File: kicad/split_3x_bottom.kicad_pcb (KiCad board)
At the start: 2 copper layers, 127.3 x 121.2 mm, 4 parts

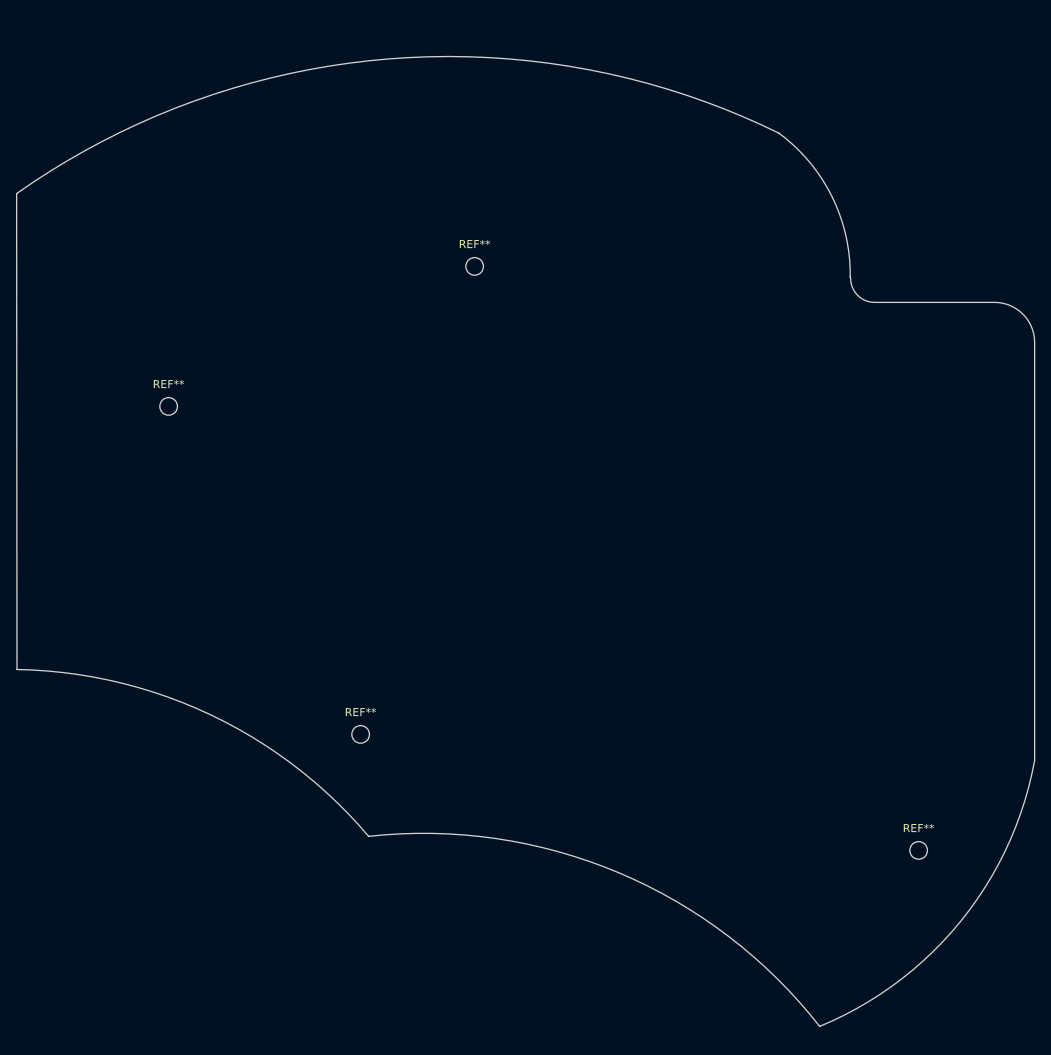
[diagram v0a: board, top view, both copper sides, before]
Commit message: added support for the pimoroni trackball breakout, changed a bunch of things, rewired the pcb, changed the bottom plate to be prettier, added some silkscreen, changed the position of one of the mounting holes, changed the angle of the trrs jacks to be properly aligned, changed the top plate to look better
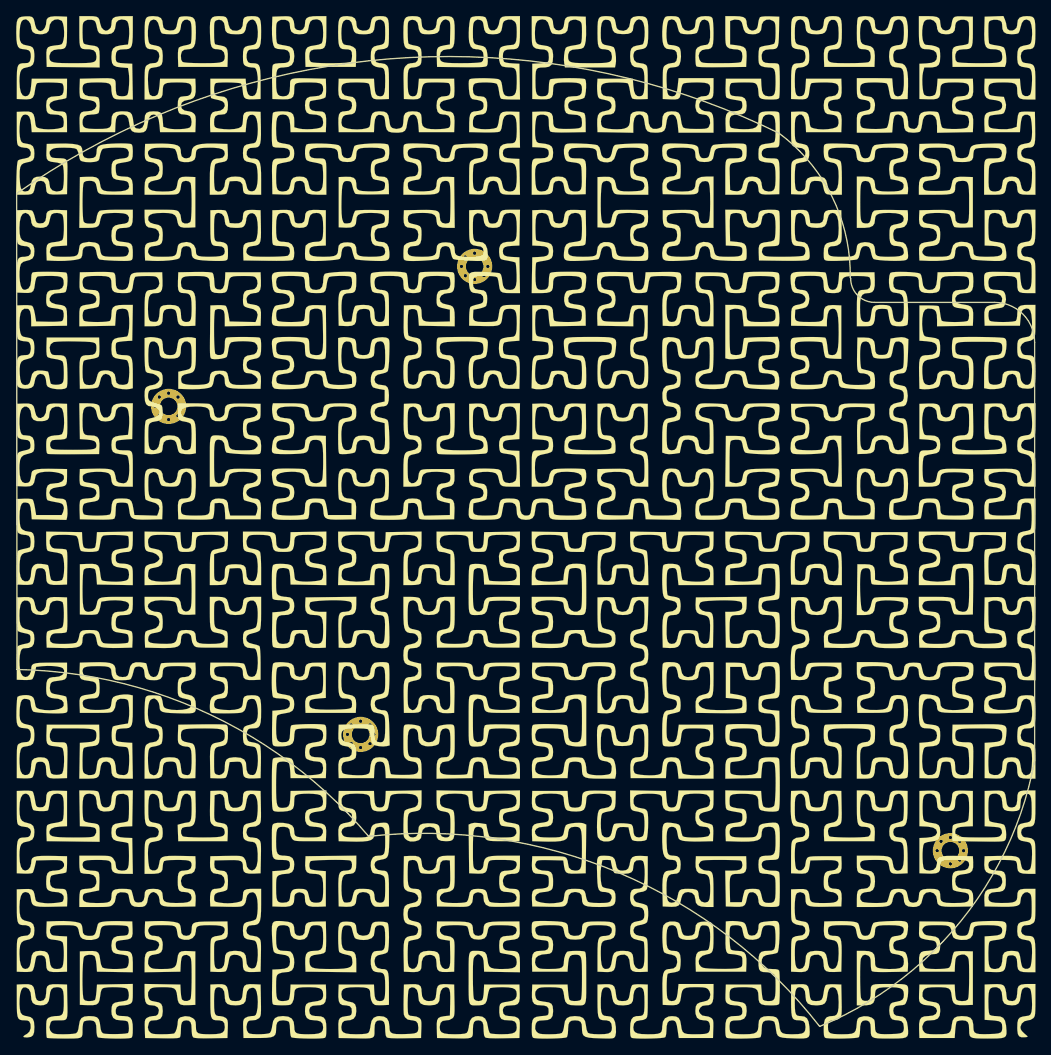
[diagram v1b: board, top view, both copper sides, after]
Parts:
- added G***: LOGO, graphics:bottom_silksreen_art, B.Cu at (141.8, 100.6)
- added G***: LOGO, graphics:bottom_silksreen_art, F.Cu at (141.6, 101.0)
-  : renamed from REF**; value MountingHole_2.2mm_M2_ISO7380 -> MountingHole_2.2mm_M2_Pad_Via; footprint MountingHole:MountingHole_2.2mm_M2_ISO7380 -> MountingHole:MountingHole_2.2mm_M2_Pad_Via (x4)
- moved   3.97 mm to (194.5, 141.3)
